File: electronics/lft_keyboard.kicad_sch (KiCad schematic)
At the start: 61 parts, among them J3 Conn_01x05_Female, J4 Conn_01x05_Male, SW1 SW_SPST, SW10 SW_SPST, SW11 SW_SPST, SW12 SW_SPST, SW13 SW_SPST, SW14 SW_SPST, SW15 SW_SPST, SW16 SW_SPST, SW17 SW_SPST, SW18 SW_SPST, SW19 SW_SPST, SW2 SW_SPST, SW20 SW_SPST, SW21 SW_SPST, SW22 SW_SPST, SW23 SW_SPST, SW24 SW_SPST, SW25 SW_SPST, SW26 SW_SPST, SW27 SW_SPST, SW28 SW_SPST, SW29 SW_SPST, SW3 SW_SPST, SW4 SW_SPST, SW5 SW_SPST, SW6 SW_SPST, SW7 SW_SPST, SW8 SW_SPST, SW9 SW_SPST, U2 PCA9675PW

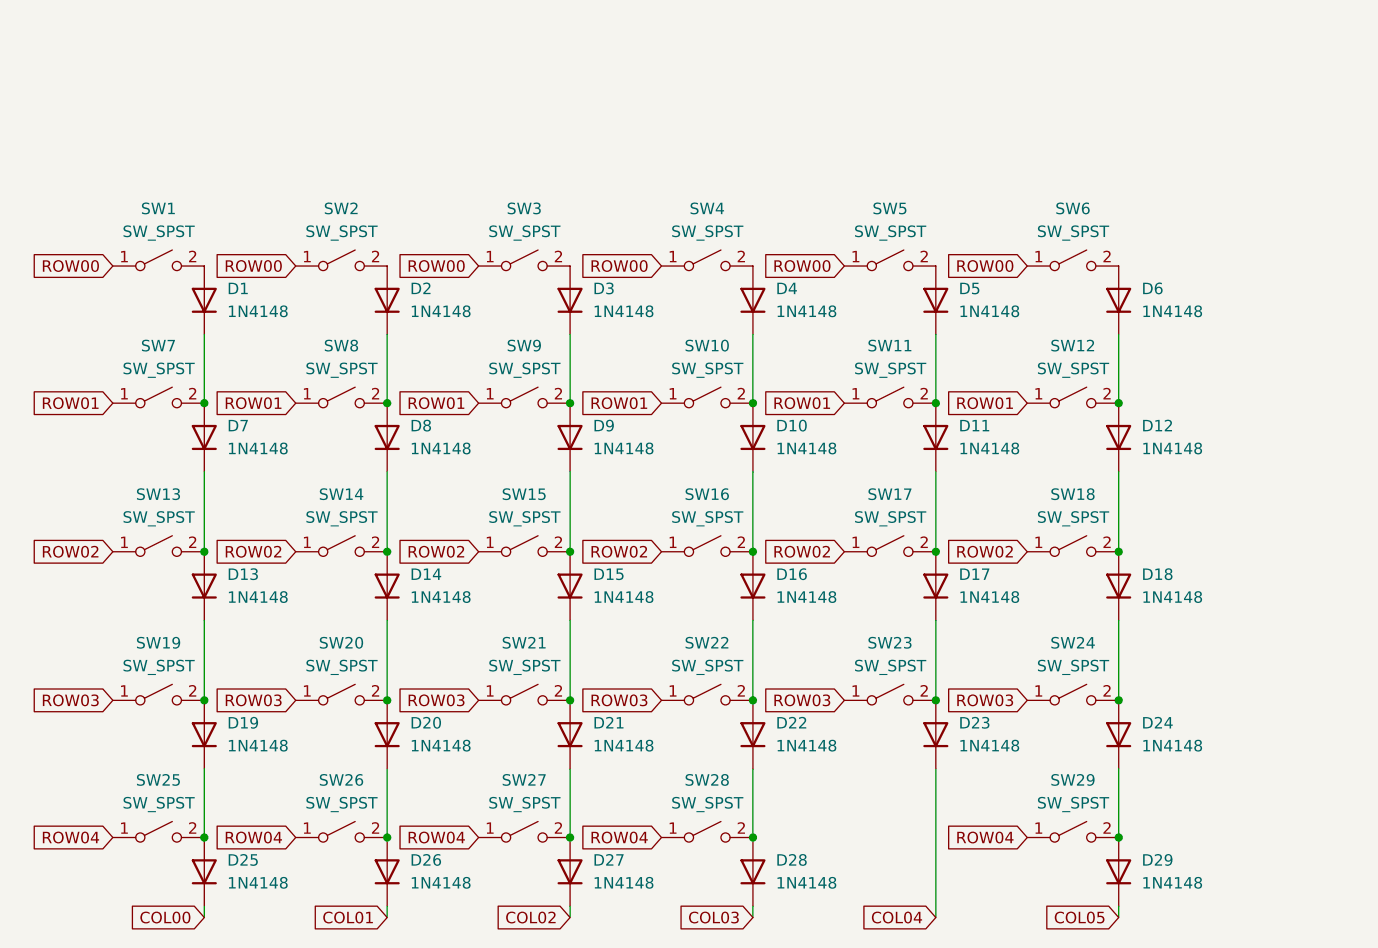
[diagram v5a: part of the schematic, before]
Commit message: reverse matrix diodes
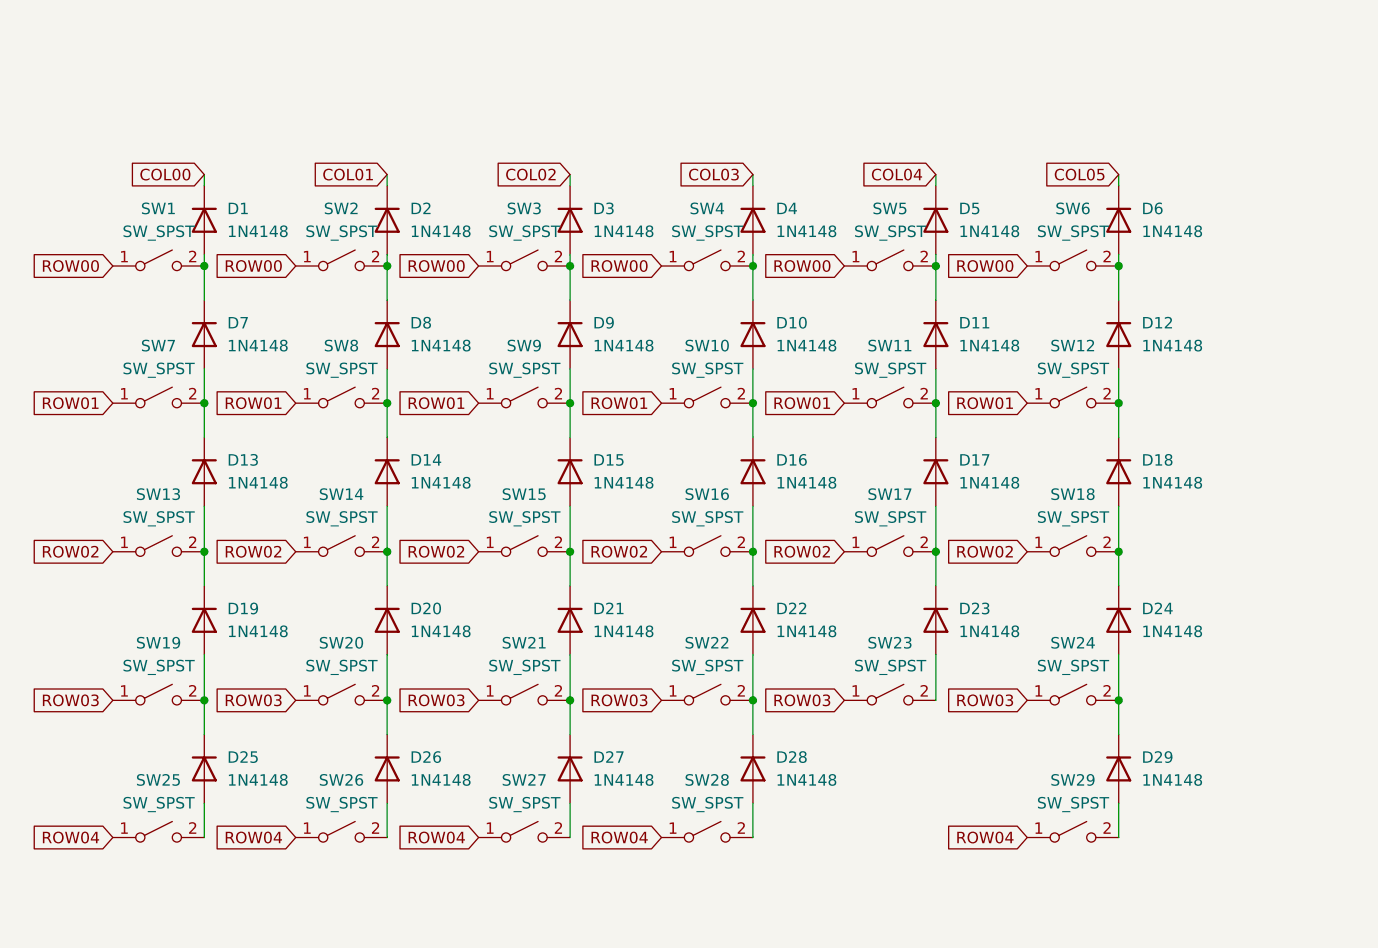
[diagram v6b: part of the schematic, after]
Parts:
- renumbered D15 to D1, D4 to D10, D5 to D11, D6 to D12, D7 to D13, D8 to D14, D9 to D15, D10 to D16, D11 to D17, D12 to D18, D27 to D19, D14 to D2, D26 to D20, D25 to D21, D16 to D22, D17 to D23, D18 to D24, D21 to D25, D20 to D26, D19 to D27, D22 to D28, D24 to D29, D13 to D3, D28 to D4, D23 to D5, D29 to D6, D1 to D7, D2 to D8, D3 to D9
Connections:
- net COL00: now also D1.1 (K); no longer D21.1 (K)
- net COL01: now also D2.1 (K); no longer D20.1 (K)
- net COL02: now also D3.1 (K); no longer D19.1 (K)
- net at D20.2 (A), D26.1 (K): now also SW20.2 (B); no longer SW26.2 (B)
- net at SW4.2 (B): now also D10.1 (K), D4.2 (A); no longer D10.2 (A)
- net at SW3.2 (B): now also D3.2 (A), D9.1 (K); no longer D9.2 (A)
- net at D21.2 (A), D27.1 (K): now also SW21.2 (B); no longer SW25.2 (B)
- net at D19.2 (A), D25.1 (K): now also SW19.2 (B); no longer SW27.2 (B)
- net at SW2.2 (B): now also D2.2 (A), D8.1 (K); no longer D8.2 (A)
- net at D12.2 (A): now also D18.1 (K), SW12.2 (B); no longer SW6.2 (B)
- net at D7.2 (A): now also D13.1 (K), SW7.2 (B); no longer SW1.2 (B)
- net at SW5.2 (B): now also D11.1 (K), D5.2 (A); no longer D11.2 (A)
- new net: D26.2 (A), SW26.2 (B)
- new net: D13.2 (A), D19.1 (K), SW13.2 (B)
- new net: D22.2 (A), D28.1 (K), SW22.2 (B)
- new net: D28.2 (A), SW28.2 (B)
- new net: D29.2 (A), SW29.2 (B)
- new net: D10.2 (A), D16.1 (K), SW10.2 (B)
- new net: D24.2 (A), D29.1 (K), SW24.2 (B)
- new net: D15.1 (K), D9.2 (A), SW9.2 (B)
- new net: D16.2 (A), D22.1 (K), SW16.2 (B)
- new net: D27.2 (A), SW27.2 (B)
- new net: D15.2 (A), D21.1 (K), SW15.2 (B)
- new net: D14.2 (A), D20.1 (K), SW14.2 (B)
- new net: D23.2 (A), SW23.2 (B)
- new net: D25.2 (A), SW25.2 (B)
- new net: D11.2 (A), D17.1 (K), SW11.2 (B)
- new net: D17.2 (A), D23.1 (K), SW17.2 (B)
- new net: D18.2 (A), D24.1 (K), SW18.2 (B)
- new net: D14.1 (K), D8.2 (A), SW8.2 (B)
- new net: D1.2 (A), D7.1 (K), SW1.2 (B)
- new net: D12.1 (K), D6.2 (A), SW6.2 (B)
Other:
- moved on the sheet: D1, D10, D11, D12, D13, D14, D15, D16, D17, D18, D19, D2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

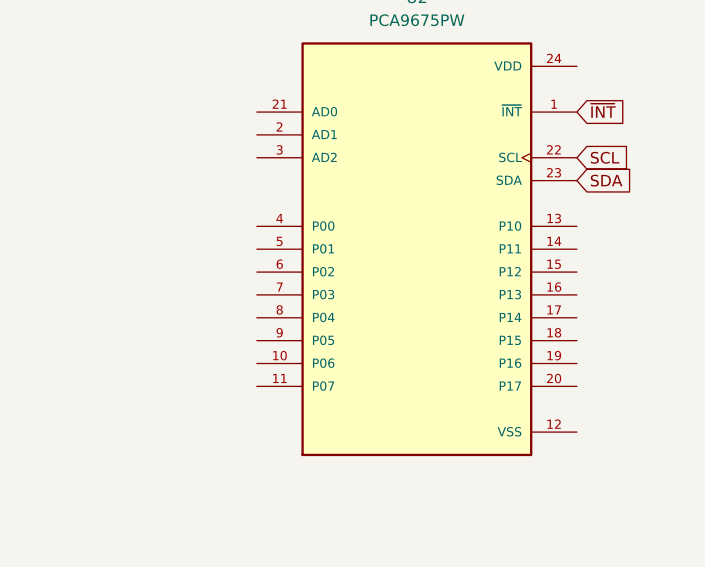
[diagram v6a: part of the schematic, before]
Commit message: connect matrix to io expander
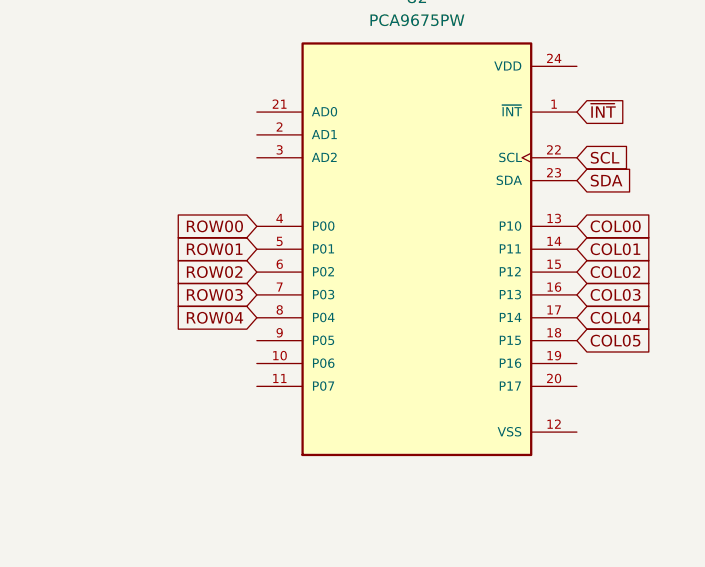
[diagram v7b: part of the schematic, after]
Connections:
- net COL00: now also U2.13 (P10)
- net COL01: now also U2.14 (P11)
- net COL02: now also U2.15 (P12)
- net COL03: now also U2.16 (P13)
- net COL04: now also U2.17 (P14)
- net COL05: now also U2.18 (P15)
- net ROW00: now also U2.4 (P00)
- net ROW01: now also U2.5 (P01)
- net ROW02: now also U2.6 (P02)
- net ROW03: now also U2.7 (P03)
- net ROW04: now also U2.8 (P04)
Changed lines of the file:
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@@
+    )
+  )
+  (global_label "COL02" (shape input) (at 224.79 48.26 0) (fields_autoplaced)
+    (effects (font (size 1.27 1.27)) (justify left))
+    (property "Intersheet References" "${INTERSHEET_REFS}" (id 0) (at 233.2507 48.3394 0)
+      (effects (font (size 1.27 1.27)) (justify left) hide)
     )
   )
@@
     )
   )
+  (global_label "ROW02" (shape input) (at 189.23 48.26 180) (fields_autoplaced)
+    (effects (font (size 1.27 1.27)) (justify right))
+    (property "Intersheet References" "${INTERSHEET_REFS}" (id 0) (at 180.3459 48.1806 0)
+      (effects (font (size 1.27 1.27)) (justify right) hide)
+    )
+  )
   (global_label "COL01" (shape input) (at 59.69 91.44 180) (fields_autoplaced)
     (effects (font (size 1.27 1.27)) (justify right))
@@
     )
   )
+  (global_label "ROW03" (shape input) (at 189.23 50.8 180) (fields_autoplaced)
+    (effects (font (size 1.27 1.27)) (justify right))
+    (property "Intersheet References" "${INTERSHEET_REFS}" (id 0) (at 180.3459 50.7206 0)
+      (effects (font (size 1.27 1.27)) (justify right) hide)
+    )
+  )
   (global_label "ROW02" (shape input) (at 29.21 133.35 180) (fields_autoplaced)
     (effects (font (size 1.27 1.27)) (justify right))
@@
     )
   )
+  (global_label "ROW00" (shape input) (at 189.23 43.18 180) (fields_autoplaced)
+    (effects (font (size 1.27 1.27)) (justify right))
+    (property "Intersheet References" "${INTERSHEET_REFS}" (id 0) (at 180.3459 43.1006 0)
+      (effects (font (size 1.27 1.27)) (justify right) hide)
+    )
+  )
+  (global_label "COL00" (shape input) (at 224.79 43.18 0) (fields_autoplaced)
+    (effects (font (size 1.27 1.27)) (justify left))
+    (property "Intersheet References" "${INTERSHEET_REFS}" (id 0) (at 233.2507 43.2594 0)
+      (effects (font (size 1.27 1.27)) (justify left) hide)
+    )
+  )
   (global_label "ROW00" (shape input) (at 130.81 101.6 180) (fields_autoplaced)
     (effects (font (size 1.27 1.27)) (justify right))
@@
     )
   )
+  (global_label "COL01" (shape input) (at 224.79 45.72 0) (fields_autoplaced)
+    (effects (font (size 1.27 1.27)) (justify left))
+    (property "Intersheet References" "${INTERSHEET_REFS}" (id 0) (at 233.2507 45.7994 0)
+      (effects (font (size 1.27 1.27)) (justify left) hide)
+    )
+  )
+  (global_label "ROW04" (shape input) (at 189.23 53.34 180) (fields_autoplaced)
+    (effects (font (size 1.27 1.27)) (justify right))
+    (property "Intersheet References" "${INTERSHEET_REFS}" (id 0) (at 180.3459 53.2606 0)
+      (effects (font (size 1.27 1.27)) (justify right) hide)
+    )
+  )
   (global_label "SCL" (shape input) (at 226.06 97.79 0) (fields_autoplaced)
     (effects (font (size 1.27 1.27)) (justify left))
@@
     )
   )
+  (global_label "ROW01" (shape input) (at 189.23 45.72 180) (fields_autoplaced)
+    (effects (font (size 1.27 1.27)) (justify right))
+    (property "Intersheet References" "${INTERSHEET_REFS}" (id 0) (at 180.3459 45.6406 0)
+      (effects (font (size 1.27 1.27)) (justify right) hide)
+    )
+  )
   (global_label "SCL" (shape input) (at 224.79 35.56 0) (fields_autoplaced)
     (effects (font (size 1.27 1.27)) (justify left))
@@
     )
   )
+  (global_label "COL03" (shape input) (at 224.79 50.8 0) (fields_autoplaced)
+    (effects (font (size 1.27 1.27)) (justify left))
+    (property "Intersheet References" "${INTERSHEET_REFS}" (id 0) (at 233.2507 50.8794 0)
+      (effects (font (size 1.27 1.27)) (justify left) hide)
+    )
+  )
+  (global_label "COL05" (shape input) (at 224.79 55.88 0) (fields_autoplaced)
+    (effects (font (size 1.27 1.27)) (justify left))
+    (property "Intersheet References" "${INTERSHEET_REFS}" (id 0) (at 233.2507 55.9594 0)
+      (effects (font (size 1.27 1.27)) (justify left) hide)
+    )
+  )
   (global_label "ROW04" (shape input) (at 49.53 165.1 180) (fields_autoplaced)
     (effects (font (size 1.27 1.27)) (justify right))
@@
     )
   )
+  (global_label "COL04" (shape input) (at 224.79 53.34 0) (fields_autoplaced)
+    (effects (font (size 1.27 1.27)) (justify left))
+    (property "Intersheet References" "${INTERSHEET_REFS}" (id 0) (at 233.2507 53.4194 0)
+      (effects (font (size 1.27 1.27)) (justify left) hide)
+    )
+  )

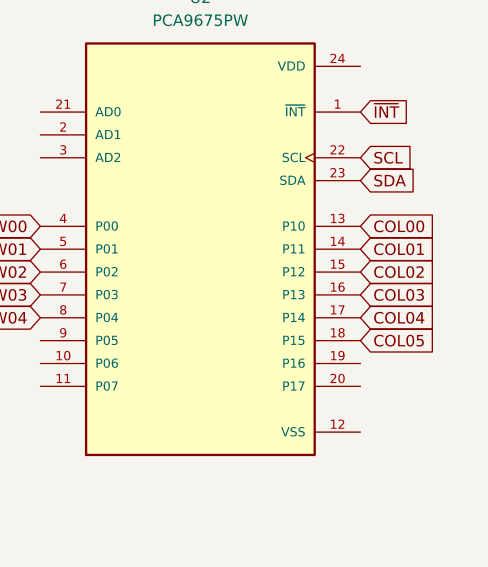
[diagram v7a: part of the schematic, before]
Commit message: connect matrix to io expander
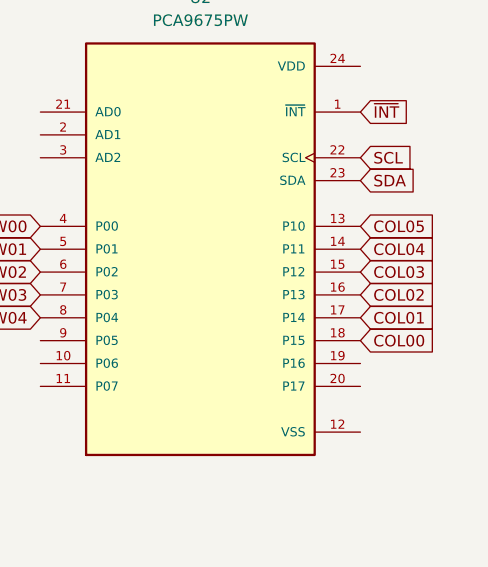
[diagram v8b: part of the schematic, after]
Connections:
- net COL00: now also U2.18 (P15); no longer U2.13 (P10)
- net COL01: now also U2.17 (P14); no longer U2.14 (P11)
- net COL02: now also U2.16 (P13); no longer U2.15 (P12)
- net COL03: now also U2.15 (P12); no longer U2.16 (P13)
- net COL04: now also U2.14 (P11); no longer U2.17 (P14)
- net COL05: now also U2.13 (P10); no longer U2.18 (P15)
